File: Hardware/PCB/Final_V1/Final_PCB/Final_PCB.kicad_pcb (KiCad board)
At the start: 2 copper layers, 0 parts

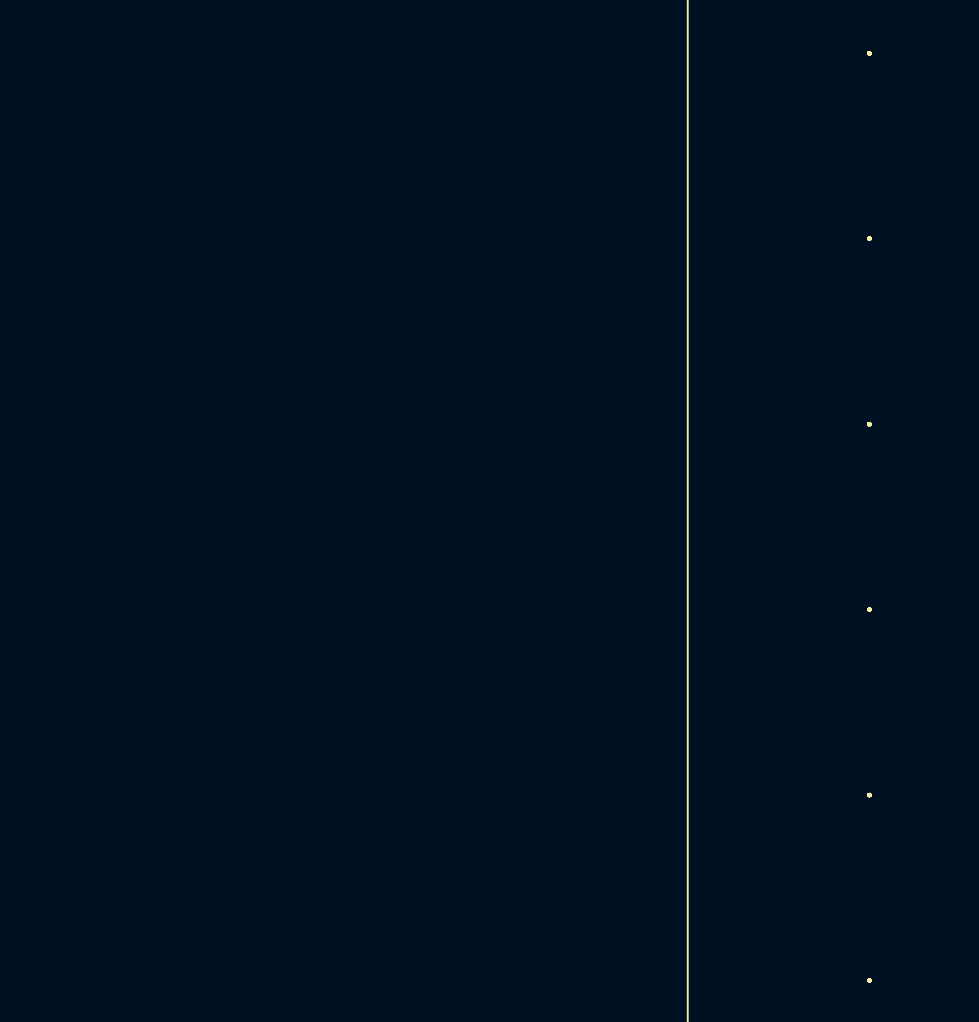
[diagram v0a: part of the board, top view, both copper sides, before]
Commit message: added footprints for BQ298010RUGR and BSC009NE2LS5IATMA1
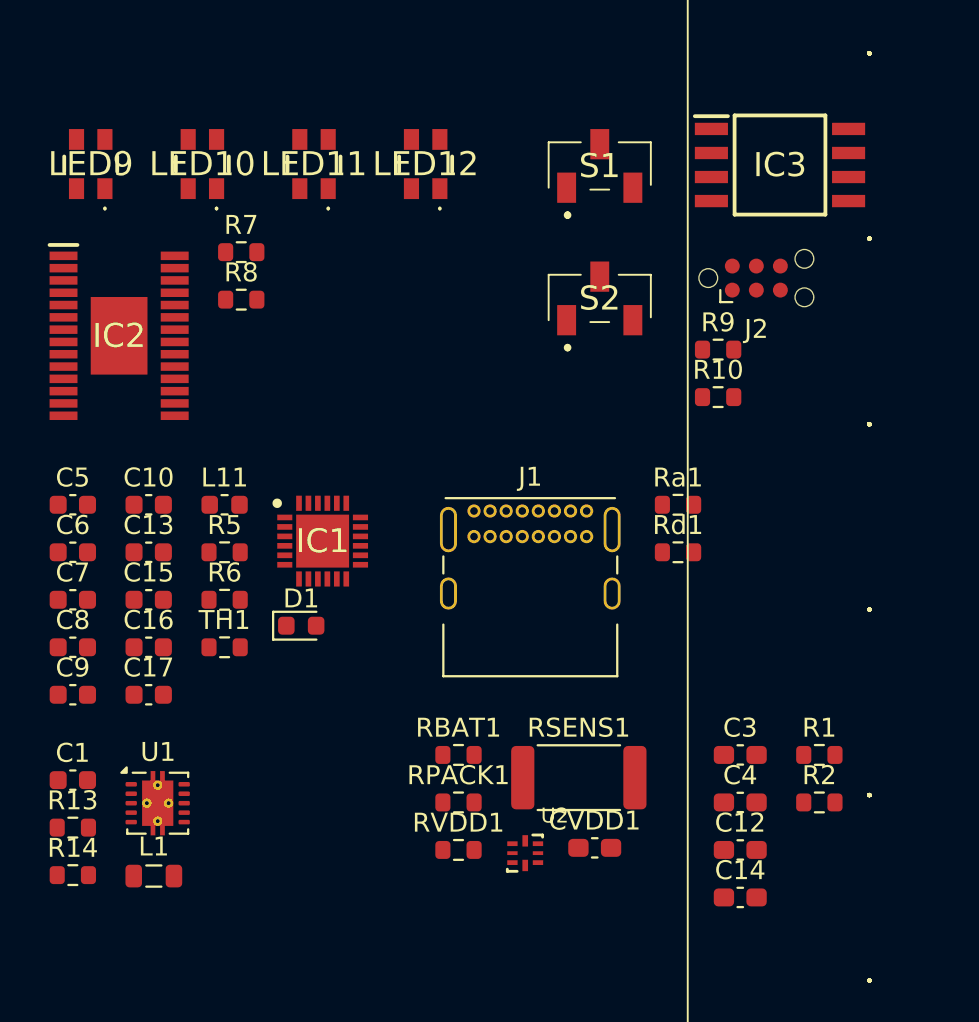
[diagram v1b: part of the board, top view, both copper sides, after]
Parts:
- added C1: 10uF, Capacitor_SMD:C_0603_1608Metric, F.Cu at (100.0, 87.6)
- added C10: 1u, Capacitor_SMD:C_0603_1608Metric, F.Cu at (104.0, 73.1)
- added C12: 0.1u, Capacitor_SMD:C_0603_1608Metric_Pad1.08x0.95mm_HandSolder, F.Cu at (135.3, 91.3)
- added C13: 4.7u, Capacitor_SMD:C_0603_1608Metric, F.Cu at (104.0, 75.6)
- added C14: 0.1u, Capacitor_SMD:C_0603_1608Metric_Pad1.08x0.95mm_HandSolder, F.Cu at (135.3, 93.8)
- added C15: 10u, Capacitor_SMD:C_0603_1608Metric, F.Cu at (104.0, 78.1)
- added C16: 10u, Capacitor_SMD:C_0603_1608Metric, F.Cu at (104.0, 80.6)
- added C17: 40u, Capacitor_SMD:C_0603_1608Metric, F.Cu at (104.0, 83.1)
- added C3: 0.1u, Capacitor_SMD:C_0603_1608Metric_Pad1.08x0.95mm_HandSolder, F.Cu at (135.3, 86.3)
- added C4: 0.1u, Capacitor_SMD:C_0603_1608Metric_Pad1.08x0.95mm_HandSolder, F.Cu at (135.3, 88.8)
- added C5: 22u, Capacitor_SMD:C_0603_1608Metric, F.Cu at (100.0, 73.1)
- added C6: 1u, Capacitor_SMD:C_0603_1608Metric, F.Cu at (100.0, 75.6)
- added C7: 4.7u, Capacitor_SMD:C_0603_1608Metric, F.Cu at (100.0, 78.1)
- added C8: 10u, Capacitor_SMD:C_0603_1608Metric, F.Cu at (100.0, 80.6)
- added C9: 22u, Capacitor_SMD:C_0603_1608Metric, F.Cu at (100.0, 83.1)
- added CVDD1: 0.1u, Capacitor_SMD:C_0603_1608Metric_Pad1.08x0.95mm_HandSolder, F.Cu at (127.6, 91.2)
- added D1: LED, LED_SMD:LED_0603_1608Metric, F.Cu at (112.1, 79.5)
- added IC1: BQ25895MRTWT, custom:QFN50P400X400X80-25N-D, F.Cu at (113.2, 75.0)
- added IC2: PCA9955BTWJ, custom:SOP65P640X110-29N, F.Cu at (102.5, 64.1)
- added IC3: ATTINY85-20SFR, custom:SOIC127P798X216-8N, F.Cu at (137.4, 55.1)
- added J1: USB_C_Receptacle_USB2.0_16P, Connector_USB:USB_C_Receptacle_GCT_USB4085, F.Cu at (121.2, 73.4)
- added J2: Conn_ARM_SWD_TagConnect_TC2030-NL, Connector:Tag-Connect_TC2030-IDC-NL_2x03_P1.27mm_Vertical, F.Cu at (136.1, 61.1)
- added L1: 2.2uH, Inductor_SMD:L_0805_2012Metric, F.Cu at (104.3, 92.7)
- added L11: 2.2u, Inductor_SMD:L_0603_1608Metric, F.Cu at (108.0, 73.1)
- added LED10: LS_E65F-BBDA-1-1, custom:LSE65FBBDA11, F.Cu at (106.8, 55.1)
- added LED11: LS_E65F-BBDA-1-1, custom:LSE65FBBDA11, F.Cu at (112.8, 55.1)
- added LED12: LS_E65F-BBDA-1-1, custom:LSE65FBBDA11, F.Cu at (118.7, 55.1)
- added LED9: LS_E65F-BBDA-1-1, custom:LSE65FBBDA11, F.Cu at (101.0, 55.1)
- added R1: 4.7k7, Resistor_SMD:R_0603_1608Metric, F.Cu at (139.5, 86.3)
- added R10: 10k, Resistor_SMD:R_0603_1608Metric, F.Cu at (134.1, 67.4)
- added R13: 1M, Resistor_SMD:R_0603_1608Metric, F.Cu at (100.0, 90.1)
- added R14: 178k, Resistor_SMD:R_0603_1608Metric, F.Cu at (100.0, 92.6)
- added R2: 4.7k, Resistor_SMD:R_0603_1608Metric, F.Cu at (139.5, 88.8)
- added R5: 322, Resistor_SMD:R_0603_1608Metric, F.Cu at (108.0, 75.6)
- added R6: 2k2, Resistor_SMD:R_0603_1608Metric, F.Cu at (108.0, 78.1)
- added R7: 23, Resistor_SMD:R_0603_1608Metric, F.Cu at (108.9, 59.7)
- added R8: 10k, Resistor_SMD:R_0603_1608Metric, F.Cu at (108.9, 62.2)
- added R9: 10k, Resistor_SMD:R_0603_1608Metric, F.Cu at (134.1, 64.9)
- added RBAT1: 330, Resistor_SMD:R_0603_1608Metric, F.Cu at (120.4, 86.3)
- added RPACK1: 100k, Resistor_SMD:R_0603_1608Metric, F.Cu at (120.4, 88.8)
- added RSENS1: 322, Resistor_SMD:R_2512_6332Metric, F.Cu at (126.7, 87.5)
- added RVDD1: 330, Resistor_SMD:R_0603_1608Metric, F.Cu at (120.4, 91.3)
- added Ra1: 5k1, Resistor_SMD:R_0603_1608Metric, F.Cu at (132.0, 73.1)
- added Rd1: 5k1, Resistor_SMD:R_0603_1608Metric, F.Cu at (132.0, 75.6)
- added S1: CAS-120A1, custom:CAS120A1, F.Cu at (127.8, 55.2)
- added S2: CAS-120A1, custom:CAS120A1, F.Cu at (127.8, 62.2)
- added TH1: Thermistor_NTC, Resistor_SMD:R_0603_1608Metric, F.Cu at (108.0, 80.6)
- added U1: TPS63000-Q1, Package_SON:Texas_DRC0010J_ThermalVias, F.Cu at (104.5, 88.8)
- added U2: BQ298xy, custom:X2QFN, F.Cu at (123.9, 91.5)

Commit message: started layouting
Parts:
- removed LED11, LED12: LS_E65F-BBDA-1-1, custom:LSE65FBBDA11
- added LED1: LS_E65F-BBDA-1-1, custom:LSE65FBBDA11, F.Cu at (142.1, 39.4)
- added LED2: LS_E65F-BBDA-1-1, custom:LSE65FBBDA11, F.Cu at (142.1, 49.2)
- added LED3: LS_E65F-BBDA-1-1, custom:LSE65FBBDA11, F.Cu at (142.1, 59.0)
- added LED4: LS_E65F-BBDA-1-1, custom:LSE65FBBDA11, F.Cu at (142.1, 68.8)
- added LED5: LS_E65F-BBDA-1-1, custom:LSE65FBBDA11, F.Cu at (142.1, 78.6)
- added LED6: LS_E65F-BBDA-1-1, custom:LSE65FBBDA11, F.Cu at (142.1, 88.4)
- added LED7: LS_E65F-BBDA-1-1, custom:LSE65FBBDA11, F.Cu at (142.1, 98.2)
- added LED8: LS_E65F-BBDA-1-1, custom:LSE65FBBDA11, F.Cu at (142.1, 108.0)
- added Q1: Q_NMOS_Depletion_DSG, custom:MOSFET_BSC093N04LSGATMA1, F.Cu at (68.3, 125.6)
- added Q2: Q_NMOS_Depletion_DSG, custom:MOSFET_BSC093N04LSGATMA1, F.Cu at (57.3, 76.4)
- IC2: moved to B.Cu
- U2: footprint custom:X2QFN -> custom:QFN50P150X150X40-8N
- moved LED10 80.7 mm to (142.1, 127.6)
- moved LED9 75.0 mm to (142.1, 117.8)
- moved C12 74.1 mm to (62.7, 76.3)
- moved C14 74.1 mm to (62.7, 78.9)
- moved C3 74.1 mm to (62.7, 71.3)
- moved C4 74.1 mm to (62.7, 73.8)
- moved R1 74.1 mm to (66.9, 71.3)
- moved R2 74.1 mm to (66.9, 73.8)
- moved IC3 74.1 mm to (64.8, 40.1)
- moved J2 74.1 mm to (63.6, 46.1)
- moved S1 74.1 mm to (55.3, 40.2)
- moved S2 74.1 mm to (55.3, 47.2)
- moved R10 74.1 mm to (61.6, 52.4)
- moved R9 74.1 mm to (61.6, 49.9)
- moved J1 73.6 mm to (50.7, 52.4)
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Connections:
- IC2 pad 15: Net-(IC2-LED8) -> unconnected-(IC2-LED8-Pad15)
- IC2 pad 16: Net-(IC2-LED9) -> unconnected-(IC2-LED9-Pad16)

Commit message: #4: Layout-Session-17-11-25
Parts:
- removed RSENS1: 322, Resistor_SMD:R_2512_6332Metric
- added BT1: Battery_Cell, Connector_PinHeader_2.54mm:PinHeader_1x02_P2.54mm_Vertical, B.Cu at (230.7, 78.5)
- added C11: 0.1uF, Capacitor_SMD:C_0603_1608Metric, B.Cu at (49.3, 63.6)
- added C2: 10uF, Capacitor_SMD:C_0603_1608Metric, B.Cu at (52.8, 50.9)
- added R11: 10k, Resistor_SMD:R_0603_1608Metric, B.Cu at (228.8, 93.5)
- added R12: 10k, Resistor_SMD:R_0603_1608Metric, B.Cu at (146.8, 113.5)
- added R15: 10k, Resistor_SMD:R_0603_1608Metric, B.Cu at (146.8, 115.0)
- added R16: 10k, Resistor_SMD:R_0603_1608Metric, B.Cu at (146.8, 118.0)
- added R17: 10k, Resistor_SMD:R_0603_1608Metric, B.Cu at (146.8, 116.5)
- added R18: 10k, Resistor_SMD:R_0603_1608Metric, B.Cu at (228.8, 106.0)
- added R19: 10k, Resistor_SMD:R_0603_1608Metric, B.Cu at (146.8, 112.0)
- added R3: 100, Resistor_SMD:R_0603_1608Metric, B.Cu at (29.9, 70.1)
- added R4: 10k, Resistor_SMD:R_0603_1608Metric, B.Cu at (228.8, 91.0)
- added TP1: TestPoint, TestPoint:TestPoint_Pad_1.5x1.5mm, B.Cu at (149.7, 116.3)
- added TP10: TestPoint, TestPoint:TestPoint_Pad_1.5x1.5mm, B.Cu at (221.5, 105.7)
- added TP11: TestPoint, TestPoint:TestPoint_Pad_1.5x1.5mm, B.Cu at (217.9, 91.5)
- added TP12: TestPoint, TestPoint:TestPoint_Pad_1.5x1.5mm, B.Cu at (217.9, 95.0)
- added TP13: TestPoint, TestPoint:TestPoint_Pad_1.5x1.5mm, B.Cu at (149.7, 121.3)
- added TP14: TestPoint, TestPoint:TestPoint_Pad_1.5x1.5mm, B.Cu at (135.5, 125.6)
- added TP15: TestPoint, TestPoint:TestPoint_Pad_1.5x1.5mm, B.Cu at (135.5, 128.1)
- added TP16: TestPoint, TestPoint:TestPoint_Pad_1.5x1.5mm, B.Cu at (214.4, 91.5)
- added TP17: TestPoint, TestPoint:TestPoint_Pad_1.5x1.5mm, B.Cu at (149.7, 113.8)
- added TP18: TestPoint, TestPoint:TestPoint_Pad_1.5x1.5mm, B.Cu at (149.7, 111.3)
- added TP19: TestPoint, TestPoint:TestPoint_Pad_1.5x1.5mm, B.Cu at (149.7, 118.8)
- added TP2: TestPoint, TestPoint:TestPoint_Pad_1.5x1.5mm, B.Cu at (225.0, 95.0)
- added TP3: TestPoint, TestPoint:TestPoint_Pad_1.5x1.5mm, B.Cu at (225.0, 98.6)
- added TP4: TestPoint, TestPoint:TestPoint_Pad_1.5x1.5mm, B.Cu at (225.0, 102.1)
- added TP5: TestPoint, TestPoint:TestPoint_Pad_1.5x1.5mm, B.Cu at (225.0, 105.7)
- added TP6: TestPoint, TestPoint:TestPoint_Pad_1.5x1.5mm, B.Cu at (221.5, 91.5)
- added TP7: TestPoint, TestPoint:TestPoint_Pad_1.5x1.5mm, B.Cu at (221.5, 95.0)
- added TP8: TestPoint, TestPoint:TestPoint_Pad_1.5x1.5mm, B.Cu at (221.5, 98.6)
- added TP9: TestPoint, TestPoint:TestPoint_Pad_1.5x1.5mm, B.Cu at (221.5, 102.1)
- added U11: MPU-6050, Sensor_Motion:InvenSense_QFN-24_4x4mm_P0.5mm, B.Cu at (138.2, 51.9)
- C1, C10, C12, C13, C14, C15, C16, C17, C3, C4, C5, C6, C8, C9, CVDD1, D1, IC1, IC3, J1, J2, L1, L11, Q1, Q2, R1, R10, R13, R14, R2, R6, R7, R8, R9, RBAT1, RPACK1, RVDD1, Ra1, Rd1, S1, S2, TH1, U1, U2: moved to B.Cu
- C7: value 4.7u -> 47u; moved to B.Cu
- R5: value 322 -> 260; moved to B.Cu
- moved C7 200.6 mm to (254.0, 127.5), turned to 180 degrees
- moved C8 200.6 mm to (254.0, 130.0), turned to 180 degrees
- moved C13 192.6 mm to (250.0, 125.0), turned to 180 degrees
- moved C15 192.6 mm to (250.0, 127.5), turned to 180 degrees
- moved C16 192.6 mm to (250.0, 130.0), turned to 180 degrees
- moved C17 192.6 mm to (250.0, 132.5), turned to 180 degrees
- moved L11 184.7 mm to (246.0, 122.5), turned to 180 degrees
- moved R5 184.7 mm to (246.0, 125.0), turned to 180 degrees
- moved R6 184.7 mm to (246.0, 127.5), turned to 180 degrees
- moved D1 176.6 mm to (241.9, 128.9), turned to 180 degrees
- moved C12 139.2 mm to (198.8, 47.0), turned to 180 degrees
- moved C14 139.2 mm to (198.8, 49.5), turned to 180 degrees
- moved C3 139.2 mm to (198.8, 42.0), turned to 180 degrees
- moved C4 139.2 mm to (198.8, 44.5), turned to 180 degrees
- moved R1 131.0 mm to (194.6, 42.0), turned to 180 degrees
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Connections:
- net Net-(IC1-ILIM) renamed /BQ25895M/ILIM
- net Net-(IC1-STAT) renamed /BQ25895M/STAT
- net Net-(IC1-SW_1) renamed /BQ25895M/SW
- C1 pad 2: FSYNC -> GND
- C12 pad 1: V3.3 -> +3.3V
- C12 pad 2: FSYNC -> GND
- C13 pad 1: FSYNC -> GND
- C14 pad 2: FSYNC -> GND
- C15 pad 2: FSYNC -> GND
- C16 pad 2: FSYNC -> GND
- C17 pad 1: FSYNC -> GND
- C3 pad 1: V3.3 -> +3.3V
- C3 pad 2: FSYNC -> GND
- C4 pad 1: FSYNC -> GND
- C6 pad 1: /BQ25895M/TS -> /BQ25895M/VBus
- C6 pad 2: FSYNC -> GND
- C8 pad 2: FSYNC -> GND
- CVDD1 pad 2: FSYNC -> GND
- IC1 pad 1: /BQ25895M/TS -> /BQ25895M/VBus
- IC1 pad 12: FSYNC -> unconnected-(IC1-~{QON}-Pad12)
- IC1 pad 17: FSYNC -> GND
- IC1 pad 18: FSYNC -> GND
- IC1 pad 24: FSYNC -> /BQ25895M/DSEL
- IC1 pad 25: FSYNC -> GND
- IC1 pad 5: unconnected-(IC1-SCL-Pad5) -> /BQ25895M/SCL
- IC1 pad 6: unconnected-(IC1-SDA-Pad6) -> /BQ25895M/SDA
- IC1 pad 7: unconnected-(IC1-INT-Pad7) -> /BQ25895M/INT
- IC1 pad 8: unconnected-(IC1-OTG-Pad8) -> /BQ25895M/OTG
- IC1 pad 9: FSYNC -> /BQ25895M/!CE
- IC2 pad 10: FSYNC -> GND
- IC2 pad 19: FSYNC -> GND
- IC2 pad 24: FSYNC -> GND
- IC2 pad 29: FSYNC -> GND
- IC2 pad 3: FSYNC -> GND
- IC2 pad 4: FSYNC -> GND
- IC2 pad 5: FSYNC -> GND
- IC3 pad 4: FSYNC -> GND
- J1 pad A1: FSYNC -> GND
- J1 pad A12: FSYNC -> GND
- J1 pad A4: /BQ25895M/TS -> /BQ25895M/VBus
- J1 pad A9: /BQ25895M/TS -> /BQ25895M/VBus
- J1 pad B1: FSYNC -> GND
- J1 pad B12: FSYNC -> GND
- J1 pad B4: /BQ25895M/TS -> /BQ25895M/VBus
- J1 pad B9: /BQ25895M/TS -> /BQ25895M/VBus
- J1 pad S1: FSYNC -> GND
- J2 pad 5: FSYNC -> GND
- R1 pad 2: V3.3 -> +3.3V
- R14 pad 2: FSYNC -> GND
- R2 pad 2: V3.3 -> +3.3V
- R5 pad 2: FSYNC -> GND
- R7 pad 1: FSYNC -> GND
- Ra1 pad 2: FSYNC -> GND
- Rd1 pad 2: FSYNC -> GND
- U1 pad 11: FSYNC -> GND
- U1 pad 3: FSYNC -> GND
- U1 pad 6: /BQ25895M/Bat_Voltage -> Net-(U1-EN)
- U1 pad 7: /BQ25895M/Bat_Voltage -> Net-(U1-EN)
- U1 pad 8: /BQ25895M/Bat_Voltage -> Net-(U1-EN)
- U1 pad 9: FSYNC -> GND
- U2 pad 3: FSYNC -> GND
- U2 pad 4: /BMS/BATT- -> GND
- U2 pad 8: /BMS/BATT- -> GND
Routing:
- net /ATTiny/SDA: track 0.00 -> 27.7 mm
- net +3.3V: track 0.00 -> 17.7 mm
- net /ATTiny/SCL: track 0.00 -> 17.2 mm
- net /ATTiny/PIN_7: track 0.00 -> 17.2 mm
- net /ATTiny/PIN_5: track 0.00 -> 17.1 mm
- net /ATTiny/PIN_1: track 0.00 -> 13.4 mm, vias 0 -> 2
- net Net-(IC2-~{RESET}): track 0.00 -> 7.36 mm
- net /ATTiny/PIN_6: track 0.00 -> 4.27 mm
- net Net-(IC2-REXT): track 0.00 -> 1.91 mm
- added copper zone on F.Cu, net +3.3V
- added copper zone on B.Cu, net GND
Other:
- board outline added: 19.2 x 94 mm

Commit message: #5: finish layout
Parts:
- moved C8 122.6 mm to (136.8, 93.9)
- moved C15 119.9 mm to (136.8, 87.8)
- moved C7 119.6 mm to (142.1, 85.3), turned to -90 degrees
- moved C16 119.4 mm to (136.8, 91.9)
- moved C17 113.9 mm to (146.3, 85.3), turned to -90 degrees
- moved C13 113.1 mm to (144.1, 85.3), turned to -90 degrees
- moved R3 112.5 mm to (142.3, 75.9)
- moved L11 112.2 mm to (140.1, 85.3), turned to -90 degrees
- moved D1 112.1 mm to (136.8, 89.8), turned to 0 degrees
- moved C2 110.5 mm to (138.7, 120.3), turned to -90 degrees
- moved R5 108.9 mm to (140.9, 96.4), turned to -90 degrees
- moved R6 103.9 mm to (149.0, 90.2)
- moved C3 99.8 mm to (136.9, 120.3), turned to -90 degrees
- moved BT1 99.7 mm to (138.4, 115.9), turned to 90 degrees
- moved C12 97.1 mm to (135.1, 120.3), turned to -90 degrees
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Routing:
- net GND: track 0.00 -> 176.3 mm, vias 0 -> 14
- net Net-(IC2-LED10): track 0.00 -> 86.2 mm, vias 0 -> 3
- net Net-(IC2-LED11): track 0.00 -> 77.9 mm, vias 0 -> 1
- net /BQ25895M/VBus: track 0.00 -> 70.4 mm, vias 0 -> 3
- net Net-(IC2-LED7): track 0.00 -> 63.6 mm, vias 0 -> 3
- net /BQ25895M/D+: track 0.00 -> 60.0 mm, vias 0 -> 2
- net Net-(IC2-LED6): track 0.00 -> 50.9 mm, vias 0 -> 3
- net /BQ25895M/D-: track 0.00 -> 46.5 mm, vias 0 -> 2
- net /BQ25895M/Bat_Voltage: track 0.00 -> 40.1 mm, vias 0 -> 2
- net Net-(IC2-LED5): track 0.00 -> 39.7 mm, vias 0 -> 3
- net /BQ25895M/TS: track 0.00 -> 35.3 mm
- net Net-(IC2-LED4): track 0.00 -> 31.1 mm, vias 0 -> 1
- net +3.3V: track 17.7 -> 42.8 mm, vias 0 -> 13
- net /BQ25895M/SDA: track 0.00 -> 24.7 mm, vias 0 -> 2
- net /BQ25895M/REGN: track 0.00 -> 23.9 mm
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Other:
- board text added: "1"
- board text added: "2"
- board text added: "Bremslicht 3 Version 1 20.11.2025"

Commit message: made a few pcb tweaks
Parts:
- moved Rd1 0.47 mm to (135.5, 127.8)
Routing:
- net GND: track 176.3 -> 161.2 mm
- net +3.3V: track 42.8 -> 48.9 mm, vias 13 -> 18
- net Net-(J1-CC2): track 8.29 -> 6.97 mm
